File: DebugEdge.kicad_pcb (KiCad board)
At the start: 2 copper layers, 18 x 13 mm, 5 parts, among them J1 Upstream Host Connector, J2 DebugEdge_02x05, J3 BYOP

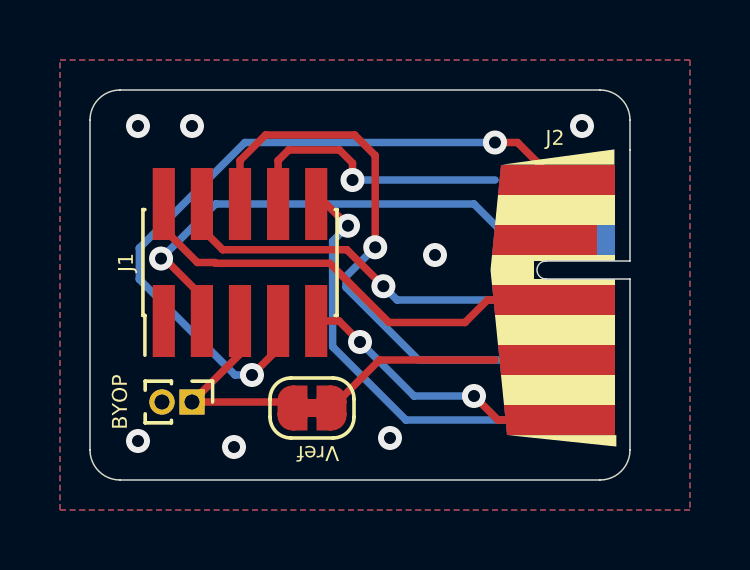
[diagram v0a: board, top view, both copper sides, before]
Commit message: Update host adapter to new footprint
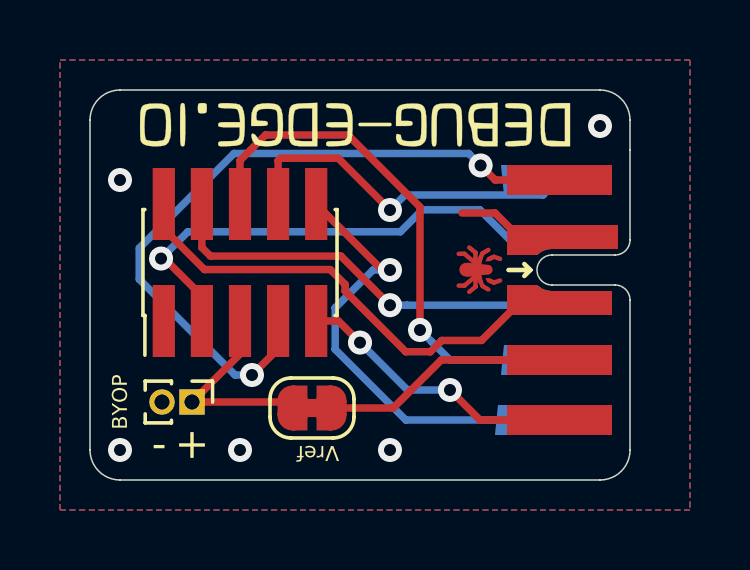
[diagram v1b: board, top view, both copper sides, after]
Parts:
- J3: value BYOP -> BYOP - Bring Your Own Power
- Ref**: moved to F.Cu
- moved Ref** 0.78 mm to (161.6, 89.0)
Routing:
- net GND: track 0.00 -> 2.37 mm, vias 7 -> 5
- net Net-(J1-Pad8): track 9.57 -> 11.9 mm
- net Net-(J2-Pad5): track 6.11 -> 8.26 mm
- net Net-(J1-Pad6): track 19.4 -> 17.8 mm
- net Net-(J1-Pad10): track 14.1 -> 15.5 mm
- net /~RESET~: track 13.6 -> 14.1 mm
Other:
- board text added: "+"
- board text added: "-"
- board text added: "Revision 1.1"
- board text removed: "Revision 1"

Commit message: change 2x5 adapter to swd/jtag pinout
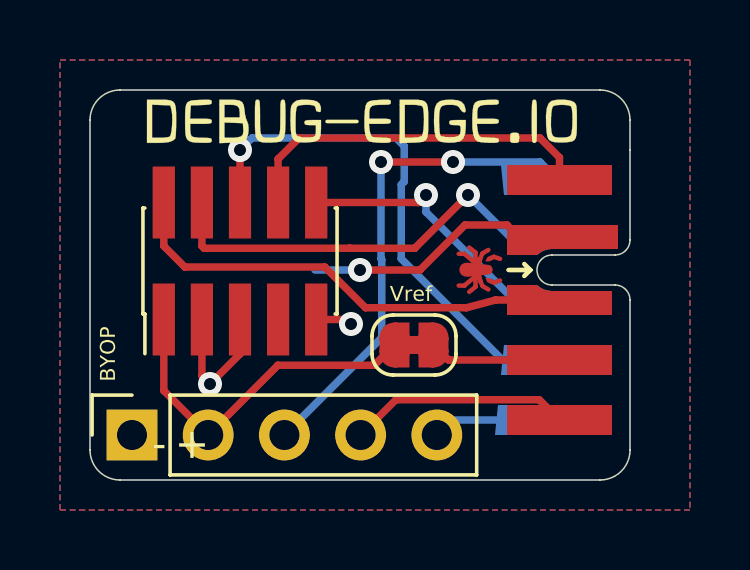
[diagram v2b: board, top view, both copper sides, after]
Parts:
- J1: value Upstream Host Connector -> Conn_02x05_Odd_Even
- J3: value BYOP - Bring Your Own Power -> Conn_01x05_Female; footprint Connector_PinHeader_1.00mm:PinHeader_1x02_P1.00mm_Vertical -> Connector_PinSocket_2.54mm:PinSocket_1x05_P2.54mm_Vertical
- moved JP1 4.00 mm to (162.8, 96.5)
- moved J3 2.28 mm to (153.4, 99.5), turned to 90 degrees
- moved Ref** 1.32 mm to (160.3, 89.2), turned to 0 degrees
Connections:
- net Net-(J1-Pad6) renamed /SWO_TDO
- J1 pad 1: GND -> VCC
- J1 pad 10: Net-(J1-Pad10) -> /~RESET~
- J1 pad 3: /SWCLK -> GND
- J1 pad 4: /~RESET~ -> /SWCLK
- J1 pad 5: VCC -> GND
- J1 pad 8: Net-(J1-Pad8) -> /TDI
- J1 pad 9: Net-(J1-Pad9) -> GND
- J2 pad 10: Net-(J1-Pad10) -> /TRACE1
- J2 pad 7: Net-(J1-Pad7) -> /TDI
- J2 pad 8: Net-(J1-Pad8) -> /TRACE_CLK
- J2 pad 9: Net-(J1-Pad9) -> /TRACE0
- J3 pad 1: VCC -> GND
- J3 pad 2: GND -> VCC
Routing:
- net Net-(J1-Pad7): track 24.0 -> 0.00 mm, vias 2 -> 0
- net /TRACE_CLK: track 0.00 -> 16.6 mm, vias 0 -> 2
- net Net-(J1-Pad10): track 15.5 -> 0.00 mm, vias 1 -> 0
- net /TDI: track 0.00 -> 12.1 mm
- net Net-(J1-Pad8): track 11.9 -> 0.00 mm, vias 1 -> 0
- net GND: track 2.37 -> 13.8 mm, vias 5 -> 3
- net Net-(J1-Pad9): track 9.48 -> 0.00 mm, vias 2 -> 0
- net /TRACE0: track 0.00 -> 7.40 mm
- net VCC: track 6.80 -> 11.9 mm
- net /TRACE1: track 0.00 -> 4.25 mm
- net Net-(J2-Pad5): track 8.26 -> 4.41 mm
- net /~RESET~: track 14.1 -> 10.2 mm
- net /SWCLK: track 16.9 -> 15.0 mm
- net /SWDIO: track 15.3 -> 14.3 mm
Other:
- board text added: "GND"
- board text added: "Revision 2.0"
- board text added: "TRACE0"
- board text added: "TRACE1"
- board text added: "TRACECLK"
- board text removed: "Revision 1.1"
